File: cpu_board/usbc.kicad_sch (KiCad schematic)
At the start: 7 parts, among them J1 USB_C_pycubed, U6 USBLC6-2SC6

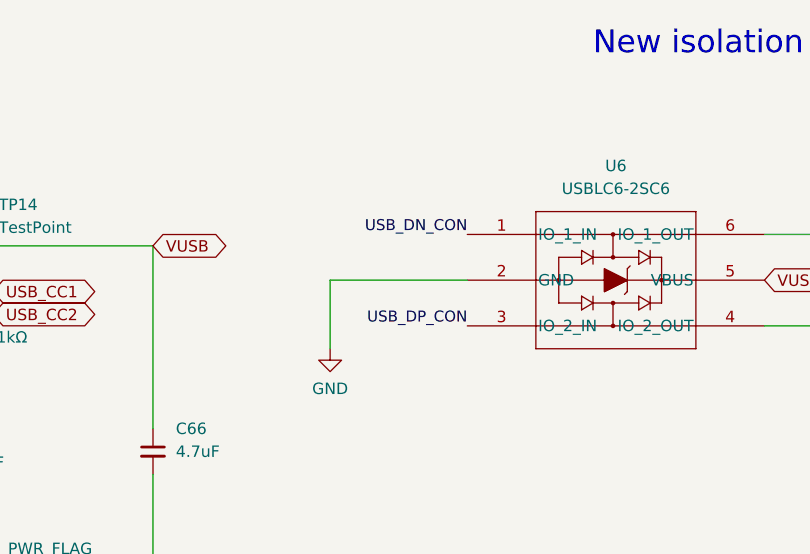
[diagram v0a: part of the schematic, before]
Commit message: clean up board2board connector and organize TODOs
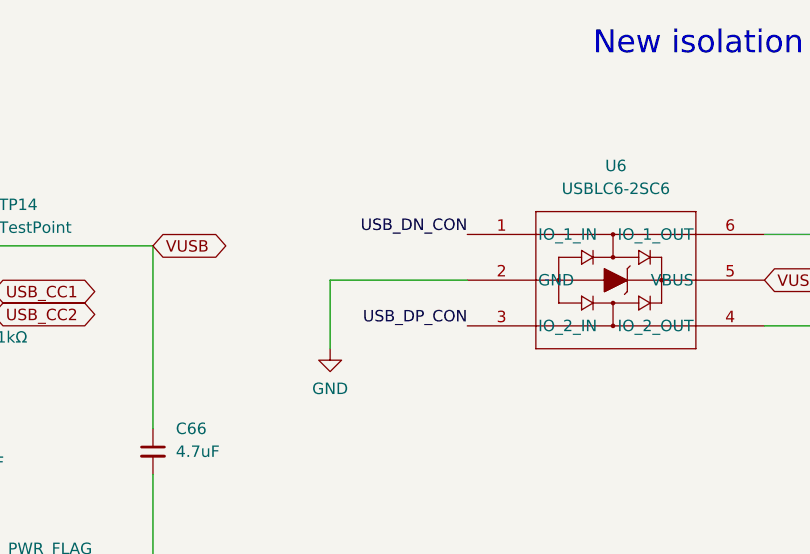
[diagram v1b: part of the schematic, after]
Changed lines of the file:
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@@
   )
   (label "USB_DN_CON" (at 226.695 133.35 180) (fields_autoplaced)
-    (effects (font (size 1.2192 1.2192)) (justify right bottom))
+    (effects (font (size 1.27 1.27)) (justify right bottom))
   )
   (label "USB_DP_CON" (at 226.695 143.51 180) (fields_autoplaced)
-    (effects (font (size 1.2192 1.2192)) (justify right bottom))
+    (effects (font (size 1.27 1.27)) (justify right bottom))
   )
   (label "USB_DP_CON" (at 146.05 152.4 0) (fields_autoplaced)

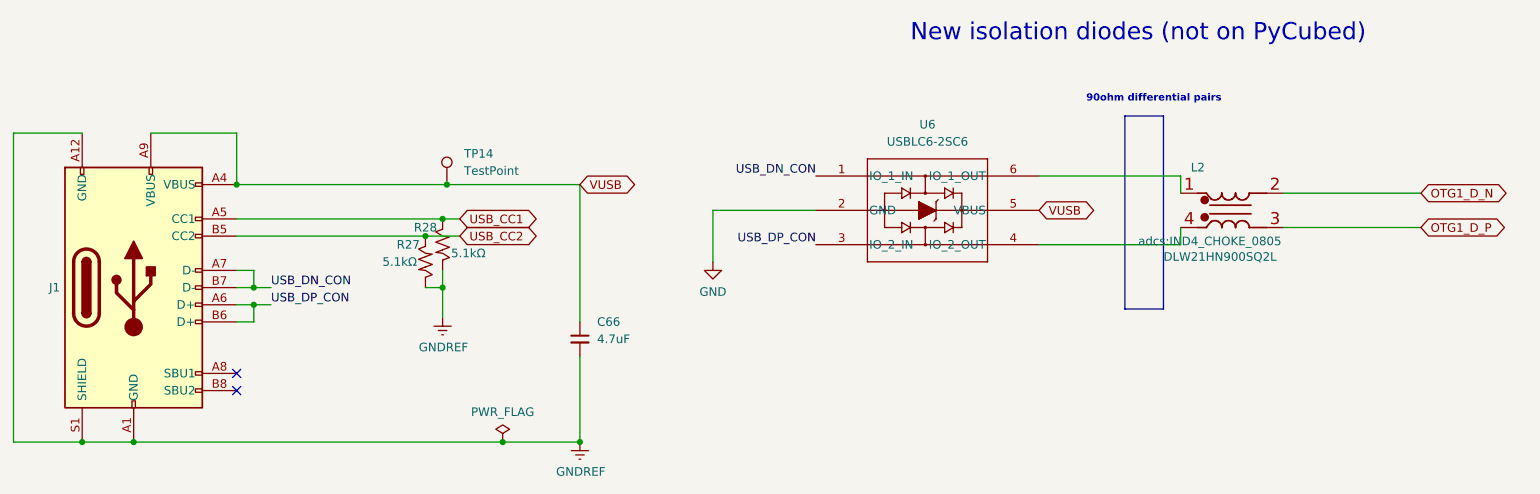
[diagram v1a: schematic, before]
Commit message: route most of power distribution
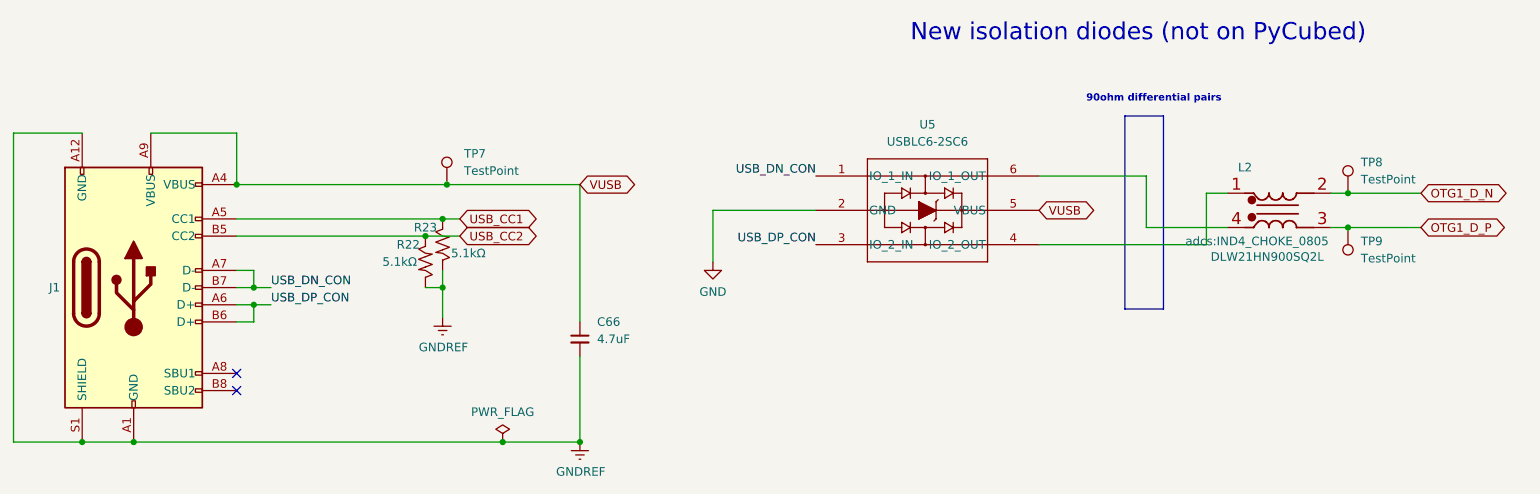
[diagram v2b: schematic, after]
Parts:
- added TP8, TP9: TestPoint, symbol Connector:TestPoint
- TP7: renamed from TP14; footprint TestPoint:TestPoint_Pad_1.5x1.5mm -> TestPoint:TestPoint_Pad_1.0x1.0mm; JLCPCB P/N (none) -> C221678
- renumbered R27 to R22, R28 to R23, U6 to U5
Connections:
- net OTG1_D_N: now also TP8.1
- net OTG1_D_P: now also TP9.1
- net at U5.4 (IO_2_OUT): now also L2.1; no longer L2.4
- net at U5.6 (IO_1_OUT): now also L2.4; no longer L2.1
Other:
- moved on the sheet: L2

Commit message: floorplan complete
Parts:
- removed TP7: TestPoint, TestPoint:TestPoint_Pad_1.0x1.0mm, symbol Connector:TestPoint
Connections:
- net USB_DN_CON renamed USB_CON_DN
- net USB_DP_CON renamed USB_CON_DP
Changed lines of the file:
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@@
   (junction (at 125.73 172.72) (diameter 0) (color 0 0 0 0)
-  )
-  (junction (at 172.085 134.62) (diameter 0) (color 0 0 0 0)
   )
   (junction (at 143.51 149.86) (diameter 0) (color 0 0 0 0)
@@
     (stroke (width 0) (type default))
   )
-  (wire (pts (xy 172.085 134.62) (xy 140.97 134.62))
+  (wire (pts (xy 140.97 134.62) (xy 191.77 134.62))
     (stroke (width 0) (type default))
   )
@@
   )
   (wire (pts (xy 275.59 140.97) (xy 287.655 140.97))
-    (stroke (width 0) (type default))
-  )
-  (wire (pts (xy 191.77 134.62) (xy 172.085 134.62))
     (stroke (width 0) (type default))
   )
@@
     (effects (font (size 1.0668 1.0668) (thickness 0.2134) bold) (justify left bottom))
   )
-  (label "USB_DN_CON" (at 146.05 149.86 0) (fields_autoplaced)
+  (label "USB_CON_DN" (at 146.05 149.86 0) (fields_autoplaced)
     (effects (font (size 1.27 1.27)) (justify left bottom))
   )
-  (label "USB_DN_CON" (at 226.695 133.35 180) (fields_autoplaced)
+  (label "USB_CON_DN" (at 226.695 133.35 180) (fields_autoplaced)
     (effects (font (size 1.27 1.27)) (justify right bottom))
   )
-  (label "USB_DP_CON" (at 226.695 143.51 180) (fields_autoplaced)
+  (label "USB_CON_DP" (at 226.695 143.51 180) (fields_autoplaced)
     (effects (font (size 1.27 1.27)) (justify right bottom))
   )
-  (label "USB_DP_CON" (at 146.05 152.4 0) (fields_autoplaced)
+  (label "USB_CON_DP" (at 146.05 152.4 0) (fields_autoplaced)
     (effects (font (size 1.27 1.27)) (justify left bottom))
   )
@@
         )
       )
-    )
-  )
-  (symbol (lib_id "Connector:TestPoint") (at 172.085 134.62 0) (unit 1)
-    (in_bom yes) (on_board yes) (dnp no) (fields_autoplaced)
-    (property "Reference" "TP7" (at 174.625 130.048 0)
-      (effects (font (size 1.27 1.27)) (justify left))
-    )
-    (property "Value" "TestPoint" (at 174.625 132.588 0)
-      (effects (font (size 1.27 1.27)) (justify left))
-    )
-    (property "Footprint" "TestPoint:TestPoint_Pad_1.0x1.0mm" (at 177.165 134.62 0)
-      (effects (font (size 1.27 1.27)) hide)
-    )
-    (property "Datasheet" "~" (at 177.165 134.62 0)
-      (effects (font (size 1.27 1.27)) hide)
-    )
-    (property "Description" "Testpoints" (at 172.085 134.62 0)
-      (effects (font (size 1.27 1.27)) hide)
-    )
-    (property "JLCPCB P/N" "C221678" (at 172.085 134.62 0)
-      (effects (font (size 1.27 1.27)) hide)
-    )
-    (property "JLCPCB P/N Proto" "" (at 172.085 134.62 0)
-      (effects (font (size 1.27 1.27)) hide)
-    )
-    (property "DNI" "DNI" (at 172.085 134.62 0)
-      (effects (font (size 1.27 1.27)) hide)
-    )
-    (property "Footprint (for JLCPCB)" "" (at 172.085 134.62 0)
-      (effects (font (size 1.27 1.27)) hide)
-    )
-    (pin "1")
-    (instances
-      (project "cpu_board"
-        (path "/c4fd7bdd-408e-44be-b66f-e6a18a0ca6e3/db53455c-7bb1-4978-a276-1508facfd1c0"
-          (reference "TP7") (unit 1)
-        )
-      )

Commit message: continue work on fanout
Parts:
- C66: footprint Capacitor_SMD:C_0402_1005Metric -> adcs:Perfect_0402
- R22, R23: footprint Resistor_SMD:R_0402_1005Metric -> adcs:Perfect_0402
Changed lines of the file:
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@@
       (effects (font (size 1.27 1.27)) (justify left))
     )
-    (property "Footprint" "Capacitor_SMD:C_0402_1005Metric" (at 191.77 157.48 0)
+    (property "Footprint" "adcs:Perfect_0402" (at 191.77 157.48 0)
       (effects (font (size 1.27 1.27)) hide)
     )
@@
       (effects (font (size 1.27 1.27)))
     )
-    (property "Footprint" "Resistor_SMD:R_0402_1005Metric" (at 169.926 145.796 90)
+    (property "Footprint" "adcs:Perfect_0402" (at 169.926 145.796 90)
       (effects (font (size 1.27 1.27)) hide)
     )
@@
       (effects (font (size 1.27 1.27)))
     )
-    (property "Footprint" "Resistor_SMD:R_0402_1005Metric" (at 172.466 143.256 90)
+    (property "Footprint" "adcs:Perfect_0402" (at 172.466 143.256 90)
       (effects (font (size 1.27 1.27)) hide)
     )

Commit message: clean up silkscreen
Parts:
- TP8, TP9: footprint (none) -> TestPoint:TestPoint_Pad_1.0x1.0mm
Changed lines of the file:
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@@
       (effects (font (size 1.27 1.27)) (justify right))
     )
-    (property "Footprint" "" (at 300.355 140.97 0)
+    (property "Footprint" "TestPoint:TestPoint_Pad_1.0x1.0mm" (at 300.355 140.97 0)
       (effects (font (size 1.27 1.27)) hide)
     )
-    (property "Datasheet" "~" (at 300.355 140.97 0)
+    (property "Datasheet" "" (at 300.355 140.97 0)
       (effects (font (size 1.27 1.27)) hide)
     )
@@
       (effects (font (size 1.27 1.27)) (justify left))
     )
-    (property "Footprint" "" (at 310.515 135.89 0)
+    (property "Footprint" "TestPoint:TestPoint_Pad_1.0x1.0mm" (at 310.515 135.89 0)
       (effects (font (size 1.27 1.27)) hide)
     )
-    (property "Datasheet" "~" (at 310.515 135.89 0)
+    (property "Datasheet" "" (at 310.515 135.89 0)
       (effects (font (size 1.27 1.27)) hide)
     )

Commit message: soldermander 1.0 ready for review
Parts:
- C66: Voltage Rating (none) -> 10V
- TP8, TP9: DNI (none) -> DNI; now left out of the parts list
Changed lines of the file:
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@@
+      (effects (font (size 1.27 1.27)) hide)
+    )
+    (property "Voltage Rating" "10V" (at 191.77 157.48 0)
       (effects (font (size 1.27 1.27)) hide)
     )
@@
   )
   (symbol (lib_id "Connector:TestPoint") (at 305.435 140.97 180) (unit 1)
-    (in_bom yes) (on_board yes) (dnp no) (fields_autoplaced)
+    (in_bom no) (on_board yes) (dnp no) (fields_autoplaced)
     (property "Reference" "TP9" (at 307.34 143.002 0)
       (effects (font (size 1.27 1.27)) (justify right))
@@
     (property "Datasheet" "" (at 300.355 140.97 0)
       (effects (font (size 1.27 1.27)) hide)
+    )
+    (property "DNI" "DNI" (at 305.435 140.97 0)
+      (effects (font (size 1.27 1.27)) hide)
+    )
+    (property "DigiKey Part Number" "" (at 305.435 140.97 0)
+      (effects (font (size 1.27 1.27)) hide)
+    )
+    (property "Tolerance" "" (at 305.435 140.97 0)
+      (effects (font (size 1.27 1.27)))
+    )
+    (property "Power Rating" "" (at 305.435 140.97 0)
+      (effects (font (size 1.27 1.27)))
     )
     (pin "1")
@@
   )
   (symbol (lib_id "Connector:TestPoint") (at 305.435 135.89 0) (unit 1)
-    (in_bom yes) (on_board yes) (dnp no) (fields_autoplaced)
+    (in_bom no) (on_board yes) (dnp no) (fields_autoplaced)
     (property "Reference" "TP8" (at 307.34 131.318 0)
       (effects (font (size 1.27 1.27)) (justify left))
@@
       (effects (font (size 1.27 1.27)) hide)
     )
-    (pin "1")
+    (property "DNI" "DNI" (at 305.435 135.89 0)
+      (effects (font (size 1.27 1.27)) hide)
+    )
+    (property "DigiKey Part Number" "" (at 305.435 135.89 0)
+      (effects (font (size 1.27 1.27)) hide)
+    )
+    (property "Tolerance" "" (at 305.435 135.89 0)
+      (effects (font (size 1.27 1.27)))
+    )
+    (property "Power Rating" "" (at 305.435 135.89 0)
+      (effects (font (size 1.27 1.27)))
+    )
+    (pin "1")

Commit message: update
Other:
- company: (none) -> Stanford Student Space Initiative
- title: (none) -> Soldermander
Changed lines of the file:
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@@
 (kicad_sch (version 20230121) (generator eeschema)
   (paper "A3")
+  (title_block
+    (title "Soldermander")
+    (date "2024-02-27")
+    (rev "1.0")
+    (company "Stanford Student Space Initiative")
+    (comment 1 "RE: Flynn Dreilinger")
+  )
   (junction (at 305.435 140.97) (diameter 0) (color 0 0 0 0)
   )
